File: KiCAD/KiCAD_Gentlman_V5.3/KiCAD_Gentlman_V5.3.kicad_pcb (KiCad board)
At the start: 2 copper layers, 1 part, among them U1 STM32G070RBT6

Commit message: KSG : V5.3 회로도 완성, 심볼 정보 업데이트 완료(데이터시트 및 풋프린트 등), 기존 BOM과 일치 완료
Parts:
- removed U1: STM32G070RBT6, STM32G070RBT6:QFP50P1200X1200X160-64N

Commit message: KSG : V5.3B용으로 회로도 수정 및 PCB 아트웤 완료.(샘플PCB주문됨)
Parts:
- added ANT1: ANT, Custom:ANT_PATTERN, F.Cu at (175.0, 90.0)
- added C1: CAP_104Z_25V_1608, Custom:C_0603_1608Metric, F.Cu at (52.0, 43.5)
- added C13: CAP_104Z_25V_1608, Custom:C_0603_1608Metric, F.Cu at (22.0, 41.0)
- added C14: CAP_104Z_25V_1608, Custom:C_0603_1608Metric, F.Cu at (22.0, 49.0)
- added C15: CAP_220uF_6.3V_SC6.3X5.8, Custom:C_Elec_6.3x5.8, F.Cu at (27.0, 38.0)
- added C16: CAP_220uF_6.3V_SC6.3X5.8, Custom:C_Elec_6.3x5.8, F.Cu at (27.0, 46.0)
- added C17: CAP_101K_250V_2012, Custom:C_0805_2012Metric, F.Cu at (179.0, 72.5)
- added C18: CAP_220uF_6.3V_SC6.3X5.8, Custom:C_Elec_6.3x5.8, F.Cu at (85.0, 75.0)
- added C19: CAP_101K_250V_2012, Custom:C_0805_2012Metric, F.Cu at (179.0, 69.0)
- added C2: CAP_104Z_25V_1608, Custom:C_0603_1608Metric, F.Cu at (52.0, 40.5)
- added C20: CAP_103K_250V_3216, Custom:C_1206_3216Metric, F.Cu at (114.0, 75.0)
- added C21: CAP_105K_250V_4532, Custom:C_1812_4532Metric, F.Cu at (117.5, 75.0)
- added C22: CAP_105K_250V_4532, Custom:C_1812_4532Metric, F.Cu at (121.5, 75.0)
- added C23: CAP_103K_25V_1608, Custom:C_0603_1608Metric, F.Cu at (126.5, 77.0)
- added C24: CAP_101K_250V_2012, Custom:C_0805_2012Metric, F.Cu at (177.5, 40.0)
- added C25: CAP_101K_250V_2012, Custom:C_0805_2012Metric, F.Cu at (177.5, 42.0)
- added C26: CAP_101K_250V_2012, Custom:C_0805_2012Metric, F.Cu at (177.5, 44.0)
- added C27: CAP_101K_250V_2012, Custom:C_0805_2012Metric, F.Cu at (177.5, 46.0)
- added C28: CAP_101K_250V_2012, Custom:C_0805_2012Metric, F.Cu at (177.5, 48.0)
- added C29: CAP_101K_250V_2012, Custom:C_0805_2012Metric, F.Cu at (177.5, 50.0)
- added C3: CAP_104Z_25V_1608, Custom:C_0603_1608Metric, F.Cu at (52.0, 42.0)
- added C30: CAP_220uF_6.3V_SC6.3X5.8, Custom:C_Elec_6.3x5.8, F.Cu at (85.0, 60.0)
- added C31: CAP_101K_250V_2012, Custom:C_0805_2012Metric, F.Cu at (177.5, 25.0)
- added C32: CAP_101K_250V_2012, Custom:C_0805_2012Metric, F.Cu at (177.5, 27.0)
- added C33: CAP_103K_250V_3216, Custom:C_1206_3216Metric, F.Cu at (114.0, 60.0)
- added C34: CAP_105K_250V_4532, Custom:C_1812_4532Metric, F.Cu at (117.5, 60.0)
- added C35: CAP_105K_250V_4532, Custom:C_1812_4532Metric, F.Cu at (121.5, 60.0)
- added C36: CAP_101K_250V_2012, Custom:C_0805_2012Metric, F.Cu at (177.5, 29.0)
- added C37: CAP_101K_250V_2012, Custom:C_0805_2012Metric, F.Cu at (177.5, 31.0)
- added C38: CAP_103K_25V_1608, Custom:C_0603_1608Metric, F.Cu at (126.5, 62.0)
- added C39: CAP_101K_250V_2012, Custom:C_0805_2012Metric, F.Cu at (177.5, 33.0)
- added C4: CAP_104Z_25V_1608, Custom:C_0603_1608Metric, F.Cu at (44.5, 26.5)
- added C40: CAP_101K_250V_2012, Custom:C_0805_2012Metric, F.Cu at (177.5, 35.0)
- added C41: CAP_220uF_6.3V_SC6.3X5.8, Custom:C_Elec_6.3x5.8, F.Cu at (85.0, 45.0)
- added C42: CAP_103K_250V_3216, Custom:C_1206_3216Metric, F.Cu at (114.0, 45.0)
- added C43: CAP_105K_250V_4532, Custom:C_1812_4532Metric, F.Cu at (117.5, 45.0)
- added C44: CAP_105K_250V_4532, Custom:C_1812_4532Metric, F.Cu at (121.5, 45.0)
- added C45: CAP_103K_25V_1608, Custom:C_0603_1608Metric, F.Cu at (126.5, 47.0)
- added C46: CAP_220uF_6.3V_SC6.3X5.8, Custom:C_Elec_6.3x5.8, F.Cu at (85.0, 30.0)
- added C47: CAP_103K_250V_3216, Custom:C_1206_3216Metric, F.Cu at (114.0, 30.0)
- added C48: CAP_105K_250V_4532, Custom:C_1812_4532Metric, F.Cu at (117.5, 30.0)
- added C49: CAP_105K_250V_4532, Custom:C_1812_4532Metric, F.Cu at (121.5, 30.0)
- added C50: CAP_103K_25V_1608, Custom:C_0603_1608Metric, F.Cu at (126.5, 32.0)
- added C51: CAP_103K_25V_1608, Custom:C_0603_1608Metric, F.Cu at (74.0, 32.0)
- added C52: CAP_100nF_1005, Custom:C_0402_1005Metric, F.Cu at (164.0, 94.6)
- added C53: CAP_100nF_1005, Custom:C_0402_1005Metric, F.Cu at (168.5, 85.1)
- added C54: CAP_4.7uF_1005, Custom:C_0402_1005Metric, F.Cu at (161.0, 86.0)
- added C55: CAP_100nF_1005, Custom:C_0402_1005Metric, F.Cu at (161.0, 87.0)
- added C56: CAP_N.C_1005, Custom:C_0402_1005Metric, F.Cu at (172.5, 87.1)
- added C57: CAP_100nF_1005, Custom:C_0402_1005Metric, F.Cu at (172.5, 86.0)
- added C58: CAP_1uF_1005, Custom:C_0402_1005Metric, F.Cu at (164.6, 83.5)
- added C59: CAP_12pF_1005, Custom:C_0402_1005Metric, F.Cu at (173.9, 83.3)
- added C6: CAP_220uF_6.3V_SC6.3X5.8, Custom:C_Elec_6.3x5.8, F.Cu at (59.5, 103.0)
- added C60: CAP_12pF_1005, Custom:C_0402_1005Metric, F.Cu at (170.1, 83.3)
- added C61: CAP_0.8pF_1005, Custom:C_0402_1005Metric, F.Cu at (172.5, 88.6)
- added C7: CAP_104Z_25V_1608, Custom:C_0603_1608Metric, F.Cu at (64.0, 105.5)
- added D1: WR106SR-W, Custom:LED_0603_1608Metric, F.Cu at (27.0, 58.0)
- added D10: MBRAF3200T3G, Custom:D_SMA, F.Cu at (111.0, 45.0)
- added D11: MBRAF3200T3G, Custom:D_SMA, F.Cu at (111.0, 30.0)
- added D2: WR106SR-W, Custom:LED_0603_1608Metric, F.Cu at (31.0, 58.0)
- added D3: WR106SR-W, Custom:LED_0603_1608Metric, F.Cu at (35.0, 58.0)
- added D4: WR106SR-W, Custom:LED_0603_1608Metric, F.Cu at (39.0, 58.0)
- added D5: WR106SR-W, Custom:LED_0603_1608Metric, F.Cu at (43.0, 58.0)
- added D6: WR106SR-W, Custom:LED_0603_1608Metric, F.Cu at (47.0, 58.0)
- added D7: WR106SR-W, Custom:LED_0603_1608Metric, F.Cu at (51.0, 58.0)
- added D8: MBRAF3200T3G, Custom:D_SMA, F.Cu at (111.0, 75.0)
- added D9: MBRAF3200T3G, Custom:D_SMA, F.Cu at (111.0, 60.0)
- added FET1: FDT86246L, Custom:SOT-223-3_TabPin2, F.Cu at (96.0, 75.0)
- added FET2: FDT86246L, Custom:SOT-223-3_TabPin2, F.Cu at (96.0, 60.0)
- added FET3: FDT86246L, Custom:SOT-223-3_TabPin2, F.Cu at (96.0, 45.0)
- added FET4: FDT86246L, Custom:SOT-223-3_TabPin2, F.Cu at (96.0, 30.0)
- added J1: PinHeader2.54mm_7, Custom:PinHeader_1x07_P2.54mm_Vertical, F.Cu at (42.0, 23.0)
- added J2: 12505WR-02, Custom:12505WR-02, F.Cu at (82.5, 102.5)
- added J4: USB-TYPE-C-31-M-17, Custom:TYPE-C-31-M-17-1, F.Cu at (32.5, 19.0)
- added J5: 12505WS-09, Custom:12505WS-09, F.Cu at (185.0, 67.5)
- added J6: 12505WS-08, Custom:12505WS-08, F.Cu at (185.1, 39.5)
- added J7: PinHeader2.54mm_5, Custom:PinHeader_1x05_P2.54mm_Vertical, F.Cu at (59.8, 23.0)
- added J8: PinHeader2.54mm_2, Custom:PinHeader_1x02_P2.54mm_Vertical, F.Cu at (93.0, 105.5)
- added JP1: PinHeader2.54mm-2-Jumper, Custom:PinHeader_1x02_P2.54mm_Vertical, F.Cu at (157.0, 82.2)
- added JP2: PinHeader2.54mm-2-Jumper, Custom:PinHeader_1x02_P2.54mm_Vertical, F.Cu at (101.2, 101.1)
- added JP3: PinHeader2.54mm-2-Jumper, Custom:PinHeader_1x02_P2.54mm_Vertical, F.Cu at (151.1, 89.7)
- added L1: SC7850D-221K, Custom:L_SC7850D-221K, F.Cu at (105.0, 75.0)
- added L10: L_10uH, Custom:L_0603_1608Metric, F.Cu at (151.2, 95.2)
- added L11: L_15nH, Custom:L_0402_1005Metric, F.Cu at (150.7, 96.4)
- added L2: SC7850D-221K, Custom:L_SC7850D-221K, F.Cu at (105.0, 60.0)
- added L3: SC7850D-221K, Custom:L_SC7850D-221K, F.Cu at (105.0, 45.0)
- added L4: SC7850D-221K, Custom:L_SC7850D-221K, F.Cu at (105.0, 30.0)
- added L5: L_3.9nH, Custom:L_0402_1005Metric, F.Cu at (173.0, 90.0)
- added L6: L_10uH, Custom:L_0603_1608Metric, F.Cu at (162.9, 83.4)
- added L7: L_15nH, Custom:L_0402_1005Metric, F.Cu at (164.6, 82.4)
- added L8: L_10uH, Custom:L_0603_1608Metric, F.Cu at (129.5, 96.0)
- added L9: L_15nH, Custom:L_0402_1005Metric, F.Cu at (128.9, 97.2)
- added Q1: 2SA1981SY, Custom:SOT-23, F.Cu at (27.0, 55.5)
- added Q10: 2N5551S, Custom:SOT-23, F.Cu at (137.0, 77.0)
- added Q11: 2N5551S, Custom:SOT-23, F.Cu at (144.5, 73.0)
- added Q12: 2N5551S, Custom:SOT-23, F.Cu at (148.0, 77.0)
- added Q13: 2N5401S, Custom:SOT-23, F.Cu at (133.5, 62.0)
- added Q14: 2N5401S, Custom:SOT-23, F.Cu at (144.5, 62.0)
- added Q15: 2N5551S, Custom:SOT-23, F.Cu at (133.5, 58.0)
- added Q16: 2N5551S, Custom:SOT-23, F.Cu at (137.0, 62.0)
- added Q17: 2N5551S, Custom:SOT-23, F.Cu at (144.5, 58.0)
- added Q18: 2N5551S, Custom:SOT-23, F.Cu at (148.0, 62.0)
- added Q19: 2N5401S, Custom:SOT-23, F.Cu at (133.5, 47.0)
- added Q2: 2SA1981SY, Custom:SOT-23, F.Cu at (31.0, 55.5)
- added Q20: 2N5401S, Custom:SOT-23, F.Cu at (144.5, 47.0)
- added Q21: 2N5401S, Custom:SOT-23, F.Cu at (155.5, 47.0)
- added Q22: 2N5401S, Custom:SOT-23, F.Cu at (166.5, 47.0)
- added Q23: 2N5551S, Custom:SOT-23, F.Cu at (133.5, 43.0)
- added Q24: 2N5551S, Custom:SOT-23, F.Cu at (137.0, 47.0)
- added Q25: 2N5551S, Custom:SOT-23, F.Cu at (144.5, 43.0)
- added Q26: 2N5551S, Custom:SOT-23, F.Cu at (148.0, 47.0)
- added Q27: 2N5551S, Custom:SOT-23, F.Cu at (155.5, 43.0)
- added Q28: 2N5551S, Custom:SOT-23, F.Cu at (159.0, 47.0)
- added Q29: 2N5551S, Custom:SOT-23, F.Cu at (166.5, 43.0)
- added Q3: 2SA1981SY, Custom:SOT-23, F.Cu at (35.0, 55.5)
- added Q30: 2N5551S, Custom:SOT-23, F.Cu at (170.0, 47.0)
- added Q31: 2N5401S, Custom:SOT-23, F.Cu at (133.5, 32.0)
- added Q32: 2N5401S, Custom:SOT-23, F.Cu at (144.5, 32.0)
- added Q33: 2N5401S, Custom:SOT-23, F.Cu at (155.5, 32.0)
- added Q34: 2N5401S, Custom:SOT-23, F.Cu at (166.5, 32.0)
- added Q35: 2N5551S, Custom:SOT-23, F.Cu at (133.5, 28.0)
- added Q36: 2N5551S, Custom:SOT-23, F.Cu at (137.0, 32.0)
- added Q37: 2N5551S, Custom:SOT-23, F.Cu at (144.5, 28.0)
- added Q38: 2N5551S, Custom:SOT-23, F.Cu at (148.0, 32.0)
- added Q39: 2N5551S, Custom:SOT-23, F.Cu at (155.5, 28.0)
- added Q4: 2SA1981SY, Custom:SOT-23, F.Cu at (39.0, 55.5)
- added Q40: 2N5551S, Custom:SOT-23, F.Cu at (159.0, 32.0)
- added Q41: 2N5551S, Custom:SOT-23, F.Cu at (166.5, 28.0)
- added Q42: 2N5551S, Custom:SOT-23, F.Cu at (170.0, 32.0)
- added Q5: 2SA1981SY, Custom:SOT-23, F.Cu at (43.0, 55.5)
- added Q6: 2SA1981SY, Custom:SOT-23, F.Cu at (47.0, 55.5)
- added Q7: 2N5401S, Custom:SOT-23, F.Cu at (133.5, 77.0)
- added Q8: 2N5401S, Custom:SOT-23, F.Cu at (144.5, 77.0)
- added Q9: 2N5551S, Custom:SOT-23, F.Cu at (133.5, 73.0)
- added R1: R_10KJ, Custom:R_0603_1608Metric, F.Cu at (46.0, 26.5)
- added R100: R_1KF, Custom:R_0603_1608Metric, F.Cu at (151.5, 43.0)
- added R101: R_100KJ, Custom:R_0603_1608Metric, F.Cu at (150.0, 43.0)
- added R102: R_100KJ, Custom:R_0603_1608Metric, F.Cu at (158.0, 43.0)
- added R103: R_1KF, Custom:R_0603_1608Metric, F.Cu at (162.5, 43.0)
- added R104: R_100KJ, Custom:R_0603_1608Metric, F.Cu at (161.0, 43.0)
- added R105: R_100KJ, Custom:R_0603_1608Metric, F.Cu at (169.0, 43.0)
- added R106: R_1KF, Custom:R_0603_1608Metric, F.Cu at (173.5, 43.0)
- added R107: R_100KJ, Custom:R_0603_1608Metric, F.Cu at (172.0, 43.0)
- added R108: R_150KF_2012, Custom:R_0805_2012Metric, F.Cu at (125.5, 27.5)
- added R109: R_120RJ_3216, Custom:R_1206_3216Metric, F.Cu at (128.5, 30.0)
- added R11: R_1KF, Custom:R_0603_1608Metric, F.Cu at (65.5, 105.5)
- added R110: R_100KJ, Custom:R_0603_1608Metric, F.Cu at (131.0, 32.0)
- added R111: R_100KJ, Custom:R_0603_1608Metric, F.Cu at (142.0, 32.0)
- added R112: R_100KJ, Custom:R_0603_1608Metric, F.Cu at (153.0, 32.0)
- added R113: R_100KJ, Custom:R_0603_1608Metric, F.Cu at (164.0, 32.0)
- added R114: R_150KF_2012, Custom:R_0805_2012Metric, F.Cu at (125.5, 29.5)
- added R115: R_100KJ, Custom:R_0603_1608Metric, F.Cu at (131.0, 28.0)
- added R116: R_100KJ, Custom:R_0603_1608Metric, F.Cu at (142.0, 28.0)
- added R117: R_100KJ, Custom:R_0603_1608Metric, F.Cu at (153.0, 28.0)
- added R118: R_100KJ, Custom:R_0603_1608Metric, F.Cu at (164.0, 28.0)
- added R119: R_1KF, Custom:R_0603_1608Metric, F.Cu at (137.5, 28.0)
- added R12: R_1KF, Custom:R_0603_1608Metric, F.Cu at (67.0, 105.5)
- added R120: R_1KF, Custom:R_0603_1608Metric, F.Cu at (148.5, 28.0)
- added R121: R_1KF, Custom:R_0603_1608Metric, F.Cu at (159.5, 28.0)
- added R122: R_1KF, Custom:R_0603_1608Metric, F.Cu at (170.5, 28.0)
- added R123: R_100RJ, Custom:R_0603_1608Metric, F.Cu at (90.0, 31.5)
- added R124: R_100KJ, Custom:R_0603_1608Metric, F.Cu at (90.0, 28.5)
- added R125: R_8.2KF, Custom:R_0603_1608Metric, F.Cu at (124.5, 32.0)
- added R126: R_100KJ, Custom:R_0603_1608Metric, F.Cu at (136.0, 28.0)
- added R127: R_1KF, Custom:R_0603_1608Metric, F.Cu at (140.5, 28.0)
- added R128: R_100KJ, Custom:R_0603_1608Metric, F.Cu at (139.0, 28.0)
- added R129: R_100KJ, Custom:R_0603_1608Metric, F.Cu at (147.0, 28.0)
- added R13: R_1KF, Custom:R_0603_1608Metric, F.Cu at (65.5, 101.5)
- added R130: R_1KF, Custom:R_0603_1608Metric, F.Cu at (151.5, 28.0)
- added R131: R_100KJ, Custom:R_0603_1608Metric, F.Cu at (150.0, 28.0)
- added R132: R_100KJ, Custom:R_0603_1608Metric, F.Cu at (158.0, 28.0)
- added R133: R_1KF, Custom:R_0603_1608Metric, F.Cu at (162.5, 28.0)
- added R134: R_100KJ, Custom:R_0603_1608Metric, F.Cu at (161.0, 28.0)
- added R135: R_100KJ, Custom:R_0603_1608Metric, F.Cu at (169.0, 28.0)
- added R136: R_1KF, Custom:R_0603_1608Metric, F.Cu at (173.5, 28.0)
- added R137: R_100KJ, Custom:R_0603_1608Metric, F.Cu at (172.0, 28.0)
- added R138: R_0RJ_6432, Custom:R_3522_6432Metric, F.Cu at (76.0, 29.0)
- added R139: R_1KF, Custom:R_0603_1608Metric, F.Cu at (78.0, 32.0)
- added R14: R_1KF, Custom:R_0603_1608Metric, F.Cu at (67.0, 101.5)
- added R15: R_47RJ, Custom:R_0603_1608Metric, F.Cu at (63.5, 83.5)
- added R16: R_47RJ, Custom:R_0603_1608Metric, F.Cu at (62.0, 83.5)
- added R17: R_47RJ, Custom:R_0603_1608Metric, F.Cu at (60.5, 83.5)
- added R18: R_47RJ, Custom:R_0603_1608Metric, F.Cu at (59.0, 83.5)
- added R19: R_47RJ, Custom:R_0603_1608Metric, F.Cu at (57.5, 83.5)
- added R2: R_390RJ, Custom:R_0603_1608Metric, F.Cu at (27.0, 53.0)
- added R26: R_4.7KF, Custom:R_0603_1608Metric, F.Cu at (25.0, 26.5)
- added R27: R_4.7KF, Custom:R_0603_1608Metric, F.Cu at (25.0, 28.0)
- added R28: R_270RF, Custom:R_0603_1608Metric, F.Cu at (38.0, 37.0)
- added R29: R_510RF, Custom:R_0603_1608Metric, F.Cu at (41.0, 37.0)
- added R3: R_390RJ, Custom:R_0603_1608Metric, F.Cu at (31.0, 53.0)
- added R30: R_150KF_2012, Custom:R_0805_2012Metric, F.Cu at (125.5, 72.5)
- added R31: R_120RJ_3216, Custom:R_1206_3216Metric, F.Cu at (128.5, 75.0)
- added R32: R_100KJ, Custom:R_0603_1608Metric, F.Cu at (131.0, 77.0)
- added R33: R_100KJ, Custom:R_0603_1608Metric, F.Cu at (142.0, 77.0)
- added R34: R_2.7KF, Custom:R_0603_1608Metric, F.Cu at (181.5, 73.0)
- added R35: R_2.7KF, Custom:R_0603_1608Metric, F.Cu at (181.5, 71.5)
- added R36: R_2.7KF, Custom:R_0603_1608Metric, F.Cu at (181.5, 70.0)
- added R37: R_2.7KF, Custom:R_0603_1608Metric, F.Cu at (181.5, 68.5)
- added R38: R_150KF_2012, Custom:R_0805_2012Metric, F.Cu at (125.5, 74.5)
- added R39: R_100KJ, Custom:R_0603_1608Metric, F.Cu at (131.0, 73.0)
- added R4: R_390RJ, Custom:R_0603_1608Metric, F.Cu at (35.0, 53.0)
- added R40: R_100KJ, Custom:R_0603_1608Metric, F.Cu at (142.0, 73.0)
- added R41: R_1KF, Custom:R_0603_1608Metric, F.Cu at (137.5, 73.0)
- added R42: R_1KF, Custom:R_0603_1608Metric, F.Cu at (148.5, 73.0)
- added R43: R_100RJ, Custom:R_0603_1608Metric, F.Cu at (90.0, 76.5)
- added R44: R_100KJ, Custom:R_0603_1608Metric, F.Cu at (90.0, 73.5)
- added R45: R_8.2KF, Custom:R_0603_1608Metric, F.Cu at (124.5, 77.0)
- added R46: R_100KJ, Custom:R_0603_1608Metric, F.Cu at (136.0, 73.0)
- added R47: R_1KF, Custom:R_0603_1608Metric, F.Cu at (140.5, 73.0)
- added R48: R_100KJ, Custom:R_0603_1608Metric, F.Cu at (139.0, 73.0)
- added R49: R_100KJ, Custom:R_0603_1608Metric, F.Cu at (147.0, 73.0)
- added R5: R_390RJ, Custom:R_0603_1608Metric, F.Cu at (39.0, 53.0)
- added R50: R_1KF, Custom:R_0603_1608Metric, F.Cu at (151.5, 73.0)
- added R51: R_100KJ, Custom:R_0603_1608Metric, F.Cu at (150.0, 73.0)
- added R52: R_150KF_2012, Custom:R_0805_2012Metric, F.Cu at (125.5, 57.5)
- added R53: R_120RJ_3216, Custom:R_1206_3216Metric, F.Cu at (128.5, 60.0)
- added R54: R_100KJ, Custom:R_0603_1608Metric, F.Cu at (131.0, 62.0)
- added R55: R_100KJ, Custom:R_0603_1608Metric, F.Cu at (142.0, 62.0)
- added R56: R_2.7KF, Custom:R_0603_1608Metric, F.Cu at (181.4, 47.3)
- added R57: R_2.7KF, Custom:R_0603_1608Metric, F.Cu at (181.4, 45.8)
- added R58: R_2.7KF, Custom:R_0603_1608Metric, F.Cu at (181.4, 44.2)
- added R59: R_150KF_2012, Custom:R_0805_2012Metric, F.Cu at (125.5, 59.5)
- added R6: R_390RJ, Custom:R_0603_1608Metric, F.Cu at (43.0, 53.0)
- added R60: R_100KJ, Custom:R_0603_1608Metric, F.Cu at (131.0, 58.0)
- added R61: R_100KJ, Custom:R_0603_1608Metric, F.Cu at (142.0, 58.0)
- added R62: R_2.7KF, Custom:R_0603_1608Metric, F.Cu at (181.4, 42.7)
- added R63: R_2.7KF, Custom:R_0603_1608Metric, F.Cu at (181.4, 32.3)
- added R64: R_2.7KF, Custom:R_0603_1608Metric, F.Cu at (181.4, 30.8)
- added R65: R_2.7KF, Custom:R_0603_1608Metric, F.Cu at (181.4, 29.2)
- added R66: R_1KF, Custom:R_0603_1608Metric, F.Cu at (137.5, 58.0)
- added R67: R_1KF, Custom:R_0603_1608Metric, F.Cu at (148.5, 58.0)
- added R68: R_2.7KF, Custom:R_0603_1608Metric, F.Cu at (181.4, 27.7)
- added R69: R_100RJ, Custom:R_0603_1608Metric, F.Cu at (90.0, 61.5)
- added R7: R_390RJ, Custom:R_0603_1608Metric, F.Cu at (47.0, 53.0)
- added R70: R_100KJ, Custom:R_0603_1608Metric, F.Cu at (90.0, 58.5)
- added R71: R_8.2KF, Custom:R_0603_1608Metric, F.Cu at (124.5, 62.0)
- added R72: R_100KJ, Custom:R_0603_1608Metric, F.Cu at (136.0, 58.0)
- added R73: R_1KF, Custom:R_0603_1608Metric, F.Cu at (140.5, 58.0)
- added R74: R_100KJ, Custom:R_0603_1608Metric, F.Cu at (139.0, 58.0)
- added R75: R_100KJ, Custom:R_0603_1608Metric, F.Cu at (147.0, 58.0)
- added R76: R_1KF, Custom:R_0603_1608Metric, F.Cu at (151.5, 58.0)
- added R77: R_100KJ, Custom:R_0603_1608Metric, F.Cu at (150.0, 58.0)
- added R78: R_150KF_2012, Custom:R_0805_2012Metric, F.Cu at (125.5, 42.5)
- added R79: R_120RJ_3216, Custom:R_1206_3216Metric, F.Cu at (128.5, 45.0)
- added R80: R_100KJ, Custom:R_0603_1608Metric, F.Cu at (131.0, 47.0)
- added R81: R_100KJ, Custom:R_0603_1608Metric, F.Cu at (142.0, 47.0)
- added R82: R_100KJ, Custom:R_0603_1608Metric, F.Cu at (153.0, 47.0)
- added R83: R_100KJ, Custom:R_0603_1608Metric, F.Cu at (164.0, 47.0)
- added R84: R_150KF_2012, Custom:R_0805_2012Metric, F.Cu at (125.5, 44.5)
- added R85: R_100KJ, Custom:R_0603_1608Metric, F.Cu at (131.0, 43.0)
- added R86: R_100KJ, Custom:R_0603_1608Metric, F.Cu at (142.0, 43.0)
- added R87: R_100KJ, Custom:R_0603_1608Metric, F.Cu at (153.0, 43.0)
- added R88: R_100KJ, Custom:R_0603_1608Metric, F.Cu at (164.0, 43.0)
- added R89: R_1KF, Custom:R_0603_1608Metric, F.Cu at (137.5, 43.0)
- added R90: R_1KF, Custom:R_0603_1608Metric, F.Cu at (148.5, 43.0)
- added R91: R_1KF, Custom:R_0603_1608Metric, F.Cu at (159.5, 43.0)
- added R92: R_1KF, Custom:R_0603_1608Metric, F.Cu at (170.5, 43.0)
- added R93: R_100RJ, Custom:R_0603_1608Metric, F.Cu at (90.0, 46.5)
- added R94: R_100KJ, Custom:R_0603_1608Metric, F.Cu at (90.0, 43.5)
- added R95: R_8.2KF, Custom:R_0603_1608Metric, F.Cu at (124.5, 47.0)
- added R96: R_100KJ, Custom:R_0603_1608Metric, F.Cu at (136.0, 43.0)
- added R97: R_1KF, Custom:R_0603_1608Metric, F.Cu at (140.5, 43.0)
- added R98: R_100KJ, Custom:R_0603_1608Metric, F.Cu at (139.0, 43.0)
- added R99: R_100KJ, Custom:R_0603_1608Metric, F.Cu at (147.0, 43.0)
- added RGB1: 1615RGBC, Custom:LED_RGB_0605, F.Cu at (30.0, 67.0)
- added RGB2: 1615RGBC, Custom:LED_RGB_0605, F.Cu at (48.0, 67.0)
- added RGB3: 1615RGBC, Custom:LED_RGB_0605, F.Cu at (39.5, 77.0)
- added RGB4: 1615RGBC, Custom:LED_RGB_0605, F.Cu at (30.0, 87.0)
- added RGB5: 1615RGBC, Custom:LED_RGB_0605, F.Cu at (48.0, 87.0)
- added SW1: SW_Tact_1105, Custom:SW_PUSH_6mm_H5mm, F.Cu at (30.0, 73.0)
- added SW2: SW_Tact_1105, Custom:SW_PUSH_6mm_H5mm, F.Cu at (48.0, 73.0)
- added SW3: SW_Tact_1105, Custom:SW_PUSH_6mm_H5mm, F.Cu at (30.0, 93.0)
- added SW4: SW_Tact_1105, Custom:SW_PUSH_6mm_H5mm, F.Cu at (48.0, 93.0)
- added SW5: SW_Tact_1105, Custom:SW_PUSH_6mm_H5mm, F.Cu at (39.5, 83.0)
- added TVS1: SMBJ15A, Custom:D_SMB, F.Cu at (27.0, 32.0)
- added U1: STM32G070RBT6, Custom:LQFP-64_10x10mm_P0.5mm, F.Cu at (63.0, 43.0)
- added U3: VLN1MM04S8X, Custom:SOP-8_3.76x4.96mm_P1.27mm, F.Cu at (72.5, 104.5)
- added U5: ULN2003D1013TR, Custom:SOIC-16_3.9x9.9mm_P1.27mm, F.Cu at (59.0, 78.0)
- added U6: LMT117-ADJ, Custom:SOT-223-3_TabPin2, F.Cu at (37.0, 43.0)
- added U7: nRF52832-QFAA, Custom:QFN-48-1EP_6x6mm_P0.4mm_EP4.3x4.3mm, F.Cu at (166.5, 90.0)
- added U8: nRF52832_DM-SModule, Custom:nRF52832_DM-SModule, F.Cu at (117.0, 97.0)
- added U9: nRF52810_PLE52M, Custom:nRF52810_PLE52M, F.Cu at (142.0, 100.5)
- added Y1: Y_32MHz, Custom:Crystal_SMD_2016-4Pin_2.0x1.6mm, F.Cu at (172.0, 83.0)
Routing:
- net GNDPWR: track 0.00 -> 696.3 mm, vias 0 -> 149
- net GNDREF: track 0.00 -> 589.1 mm
- net +5V: track 0.00 -> 351.1 mm, vias 0 -> 14
- net +3.6V: track 0.00 -> 311.6 mm, vias 0 -> 4
- net RGB_G6: track 0.00 -> 250.5 mm, vias 0 -> 4
- net RGB_B6: track 0.00 -> 242.3 mm, vias 0 -> 2
- net nRF_SWDIO: track 0.00 -> 229.1 mm, vias 0 -> 8
- net RGB_R6: track 0.00 -> 225.6 mm, vias 0 -> 4
- net nRF_SWCLK: track 0.00 -> 224.3 mm, vias 0 -> 6
- net UART: track 0.00 -> 195.3 mm, vias 0 -> 11
- net RGB_COM6: track 0.00 -> 172.7 mm, vias 0 -> 2
- net CH4_P4_CTL2: track 0.00 -> 140.6 mm, vias 0 -> 2
- net CH4_P4_CTL1: track 0.00 -> 135.9 mm, vias 0 -> 2
- net CH4_P3_CTL2: track 0.00 -> 126.1 mm, vias 0 -> 2
- net CH4_P3_CTL1: track 0.00 -> 121.4 mm, vias 0 -> 2
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- added copper zone on B.Cu, net GNDPWR
- added copper zone on F.Cu, net GNDPWR
- added copper zone on F.Cu, net GNDREF
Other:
- board outline added: 170 x 90 mm
- net class Custom added: clearance 0.2, trace_width 0.25, via_dia 0.4, via_drill 0.3
- net class Custom_0402 added: clearance 0.1, trace_width 0.2, via_dia 0.4, via_drill 0.3
- net class Custom_Ch added: clearance 0.15, trace_width 0.25, via_dia 0.4, via_drill 0.3
- board text added: "3.6V"
- board text added: "5V"
- board text added: "GND"
- board text added: "Gentlman v5.3B Phyche KSG 2021-11-29"
- board text added: "NRST"
- board text added: "STMCLK"
- board text added: "STMIO"
- board text added: "UART"
- board text added: "nRFCLK"
- board text added: "nRFIO"

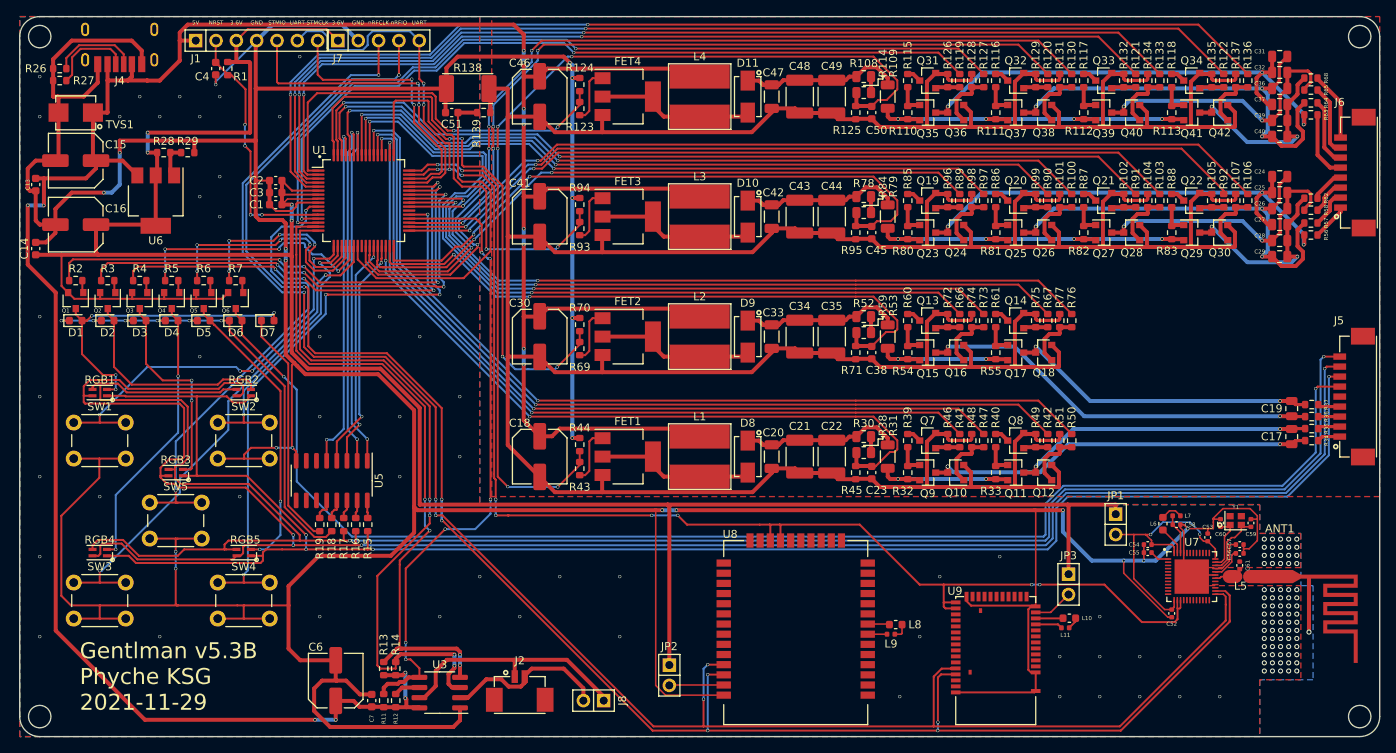
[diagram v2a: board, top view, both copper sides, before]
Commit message: KSG : 보드 수정(크리스탈 배치 문제, 점퍼추가, 이름위치오기수정, IC1번핀표시)
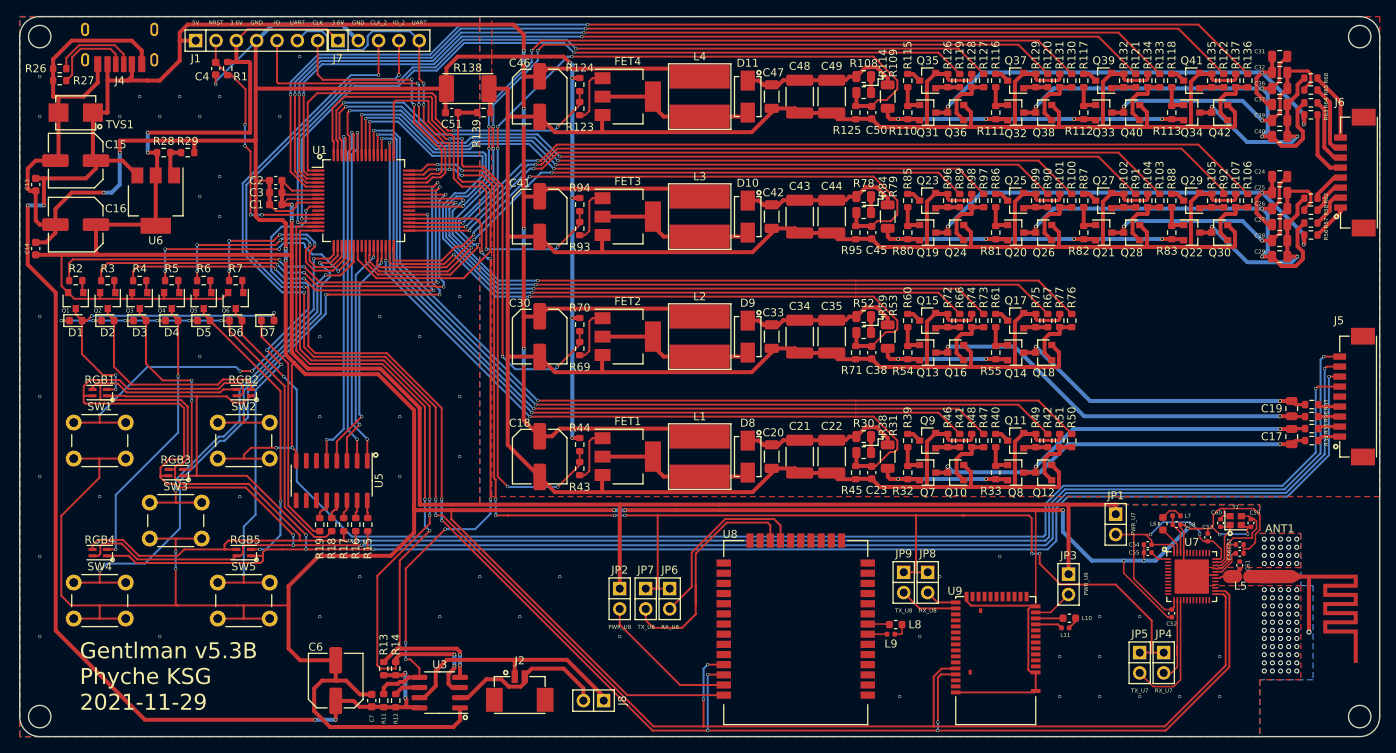
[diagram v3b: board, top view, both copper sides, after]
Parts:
- added JP4: PinHeader2.54mm-2-Jumper, Custom:PinHeader_1x02_P2.54mm_Vertical, F.Cu at (163.0, 99.5)
- added JP5: PinHeader2.54mm-2-Jumper, Custom:PinHeader_1x02_P2.54mm_Vertical, F.Cu at (160.0, 99.5)
- added JP6: PinHeader2.54mm-2-Jumper, Custom:PinHeader_1x02_P2.54mm_Vertical, F.Cu at (101.2, 91.5)
- added JP7: PinHeader2.54mm-2-Jumper, Custom:PinHeader_1x02_P2.54mm_Vertical, F.Cu at (98.2, 91.5)
- added JP8: PinHeader2.54mm-2-Jumper, Custom:PinHeader_1x02_P2.54mm_Vertical, F.Cu at (133.5, 89.5)
- added JP9: PinHeader2.54mm-2-Jumper, Custom:PinHeader_1x02_P2.54mm_Vertical, F.Cu at (130.5, 89.5)
- moved SW4 18.0 mm to (30.0, 93.0)
- moved SW3 13.8 mm to (39.5, 83.0)
- moved SW5 13.1 mm to (48.0, 93.0)
- moved JP2 11.4 mm to (95.0, 91.5)
- turned C59 to 270 degrees
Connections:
- U7 pad 14: UART -> Net-(JP4-Pad2)
- U7 pad 15: UART -> Net-(JP5-Pad2)
- U8 pad 21: UART -> Net-(JP6-Pad2)
- U8 pad 22: UART -> Net-(JP7-Pad2)
- U9 pad 25: UART -> Net-(JP8-Pad2)
- U9 pad 26: UART -> Net-(JP9-Pad2)
- Y1 pad 2: Net-(C59-Pad1) -> GNDPWR
- Y1 pad 3: (no net) -> Net-(C59-Pad1)
- Y1 pad 4: (no net) -> GNDPWR
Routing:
- net Net-(JP7-Pad2): track 0.00 -> 31.7 mm
- net GNDPWR: track 696.3 -> 719.5 mm, vias 149 -> 148
- net Net-(JP6-Pad2): track 0.00 -> 23.2 mm
- net Net-(JP5-Pad2): track 0.00 -> 16.1 mm
- net UART: track 195.3 -> 211.0 mm
- net Net-(SW3-Pad1): track 63.1 -> 49.3 mm
- net Net-(JP4-Pad2): track 0.00 -> 11.5 mm
- net Net-(JP2-Pad2): track 6.82 -> 18.1 mm
- net Net-(SW4-Pad1): track 79.5 -> 90.0 mm
- net +3.6V: track 311.6 -> 301.9 mm
- net Net-(SW5-Pad1): track 58.4 -> 66.4 mm, vias 2 -> 4
- net Net-(JP9-Pad2): track 0.00 -> 7.32 mm
- net Net-(JP8-Pad2): track 0.00 -> 4.01 mm
- net nRF_SWCLK: track 224.3 -> 228.0 mm
- net Net-(C59-Pad1): track 8.38 -> 11.7 mm
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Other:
- board text added: "CLK"
- board text added: "CLK_2"
- board text added: "IO"
- board text added: "IO_2"
- board text added: "PWR_U7"
- board text added: "PWR_U8"
- board text added: "PWR_U9"
- board text added: "RX_U7"
- board text added: "RX_U8"
- board text added: "TX_U7"
- board text added: "TX_U8"
- board text removed: "STMCLK"
- board text removed: "STMIO"
- board text removed: "nRFCLK"
- board text removed: "nRFIO"
